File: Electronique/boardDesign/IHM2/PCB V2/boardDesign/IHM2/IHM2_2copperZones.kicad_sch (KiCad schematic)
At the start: 20 parts, among them J1 Conn_01x14, SW1 SW_Push_Dual_INIT, SW2 SW_Push_Dual_START, SW3 SW_Push_Dual_PAUSE, SW4 RotaryEncoder_Switch, U1 ER_OLEDM0.91_1x-I2C

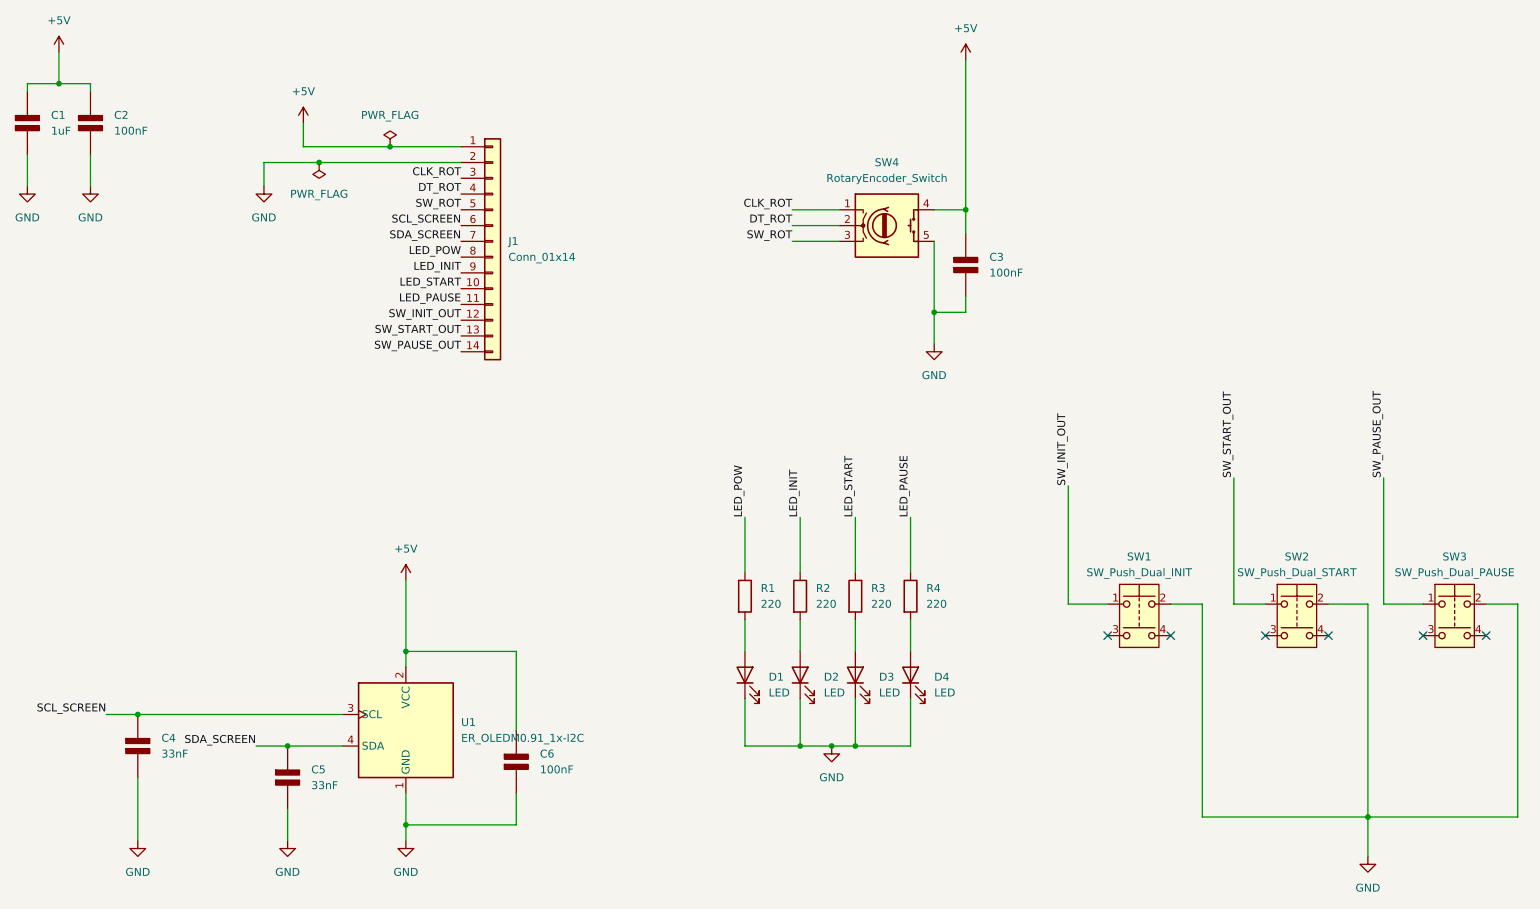
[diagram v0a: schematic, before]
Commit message: feat : creation of PCB HMI with corresponding schematics and footprints doc : created links list for online resources
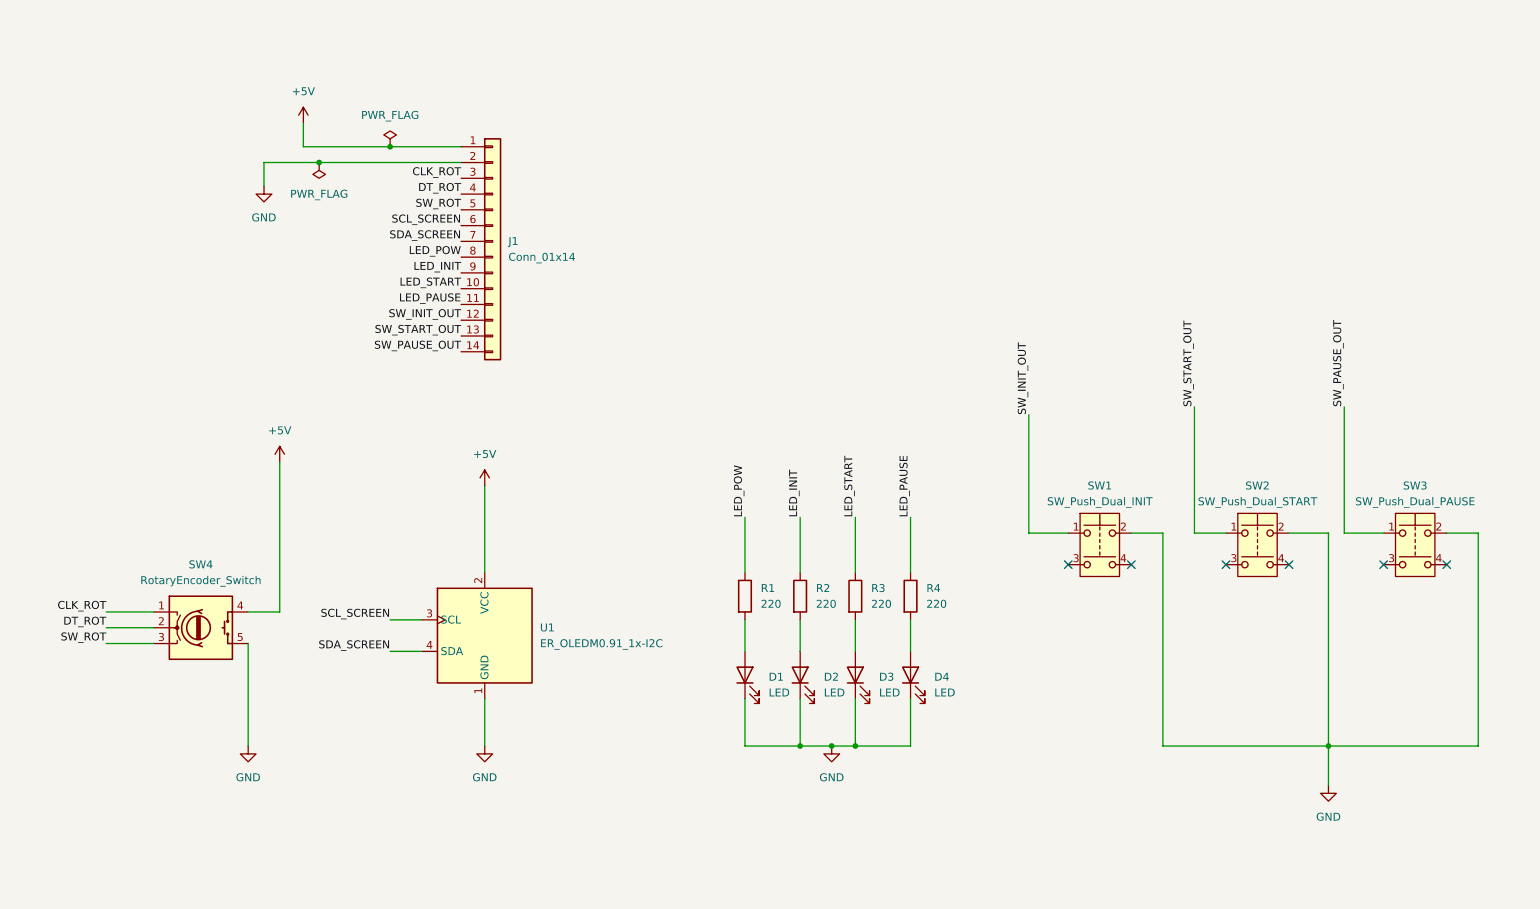
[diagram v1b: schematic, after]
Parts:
- removed C1: 1uF, Capacitor_SMD:C_1206_3216Metric, symbol PCM_Elektuur:C
- removed C2, C3, C6: 100nF, Capacitor_SMD:C_1206_3216Metric, symbol PCM_Elektuur:C
- removed C4, C5: 33nF, Capacitor_SMD:C_1206_3216Metric, symbol PCM_Elektuur:C
- R1, R2, R3, R4: footprint Resistor_SMD:R_1206_3216Metric -> Resistor_SMD:R_0805_2012Metric
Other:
- moved on the sheet: SW1, SW2, SW3, SW4, U1
